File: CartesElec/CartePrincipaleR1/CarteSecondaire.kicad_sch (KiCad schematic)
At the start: 17 parts

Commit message: small updates
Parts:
- removed J? (x2): Conn_01x04_Male, symbol Connector:Conn_01x04_Male
- removed SW? (x2): SW_SPDT, symbol Switch:SW_SPDT
- added CONN_COL2: POMPE_1, Connector_JST:JST_XH_B2B-XH-A_1x02_P2.50mm_Vertical, symbol Connector:Conn_01x02_Male
- added CONN_COL3: POMPE_2, Connector_JST:JST_XH_B2B-XH-A_1x02_P2.50mm_Vertical, symbol Connector:Conn_01x02_Male
- added CONN_COL4, CONN_TIR2: Conn_01x02_Male, Connector_JST:JST_XH_B2B-XH-A_1x02_P2.50mm_Vertical, symbol Connector:Conn_01x02_Male
- added CONN_COL5: EV_1, Connector_JST:JST_XH_B2B-XH-A_1x02_P2.50mm_Vertical, symbol Connector:Conn_01x02_Male
- added CONN_COL6: EV_2, Connector_JST:JST_XH_B2B-XH-A_1x02_P2.50mm_Vertical, symbol Connector:Conn_01x02_Male
- added J17: Conn_01x02_Male, symbol Connector:Conn_01x02_Male
- added Q1, Q2, Q3, Q4: IRLML0030, Package_TO_SOT_SMD:SOT-23, symbol Transistor_FET:IRLML0030
- added R3, R5, R6, R7: R, symbol Device:R
- gave numbers to parts that had none: 13
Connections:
- net +12V: now also CONN_COL2.1 (Pin_1), CONN_COL3.1 (Pin_1), CONN_COL5.1 (Pin_1), CONN_COL6.1 (Pin_1), J17.1 (Pin_1)
- net GND: now also CONN_COL4.2 (Pin_2), CONN_TIR2.2 (Pin_2), J17.2 (Pin_2), Q1.2 (S), Q2.2 (S), Q3.2 (S), Q4.2 (S), R3.2, R5.2, R6.2, R7.2
- net DataAX12 renamed DataAX12_TX
- new net: Q3.1 (G), R6.1
- new net: CONN_COL5.2 (Pin_2), Q3.3 (D)
- new net: CONN_COL2.2 (Pin_2), Q1.3 (D)
- new net: CONN_COL6.2 (Pin_2), Q4.3 (D)
- new net: Q4.1 (G), R7.1
- new net: CONN_COL3.2 (Pin_2), Q2.3 (D)
- new net: Q1.1 (G), R3.1
- new net: Q2.1 (G), R5.1
- new net CONTACTEUR1_GPIO: CONN_COL4.1 (Pin_1)
- new net CONTACTEUR2_GPIO: CONN_TIR2.1 (Pin_1)
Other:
- moved on the sheet: J15, J16, J19, J21

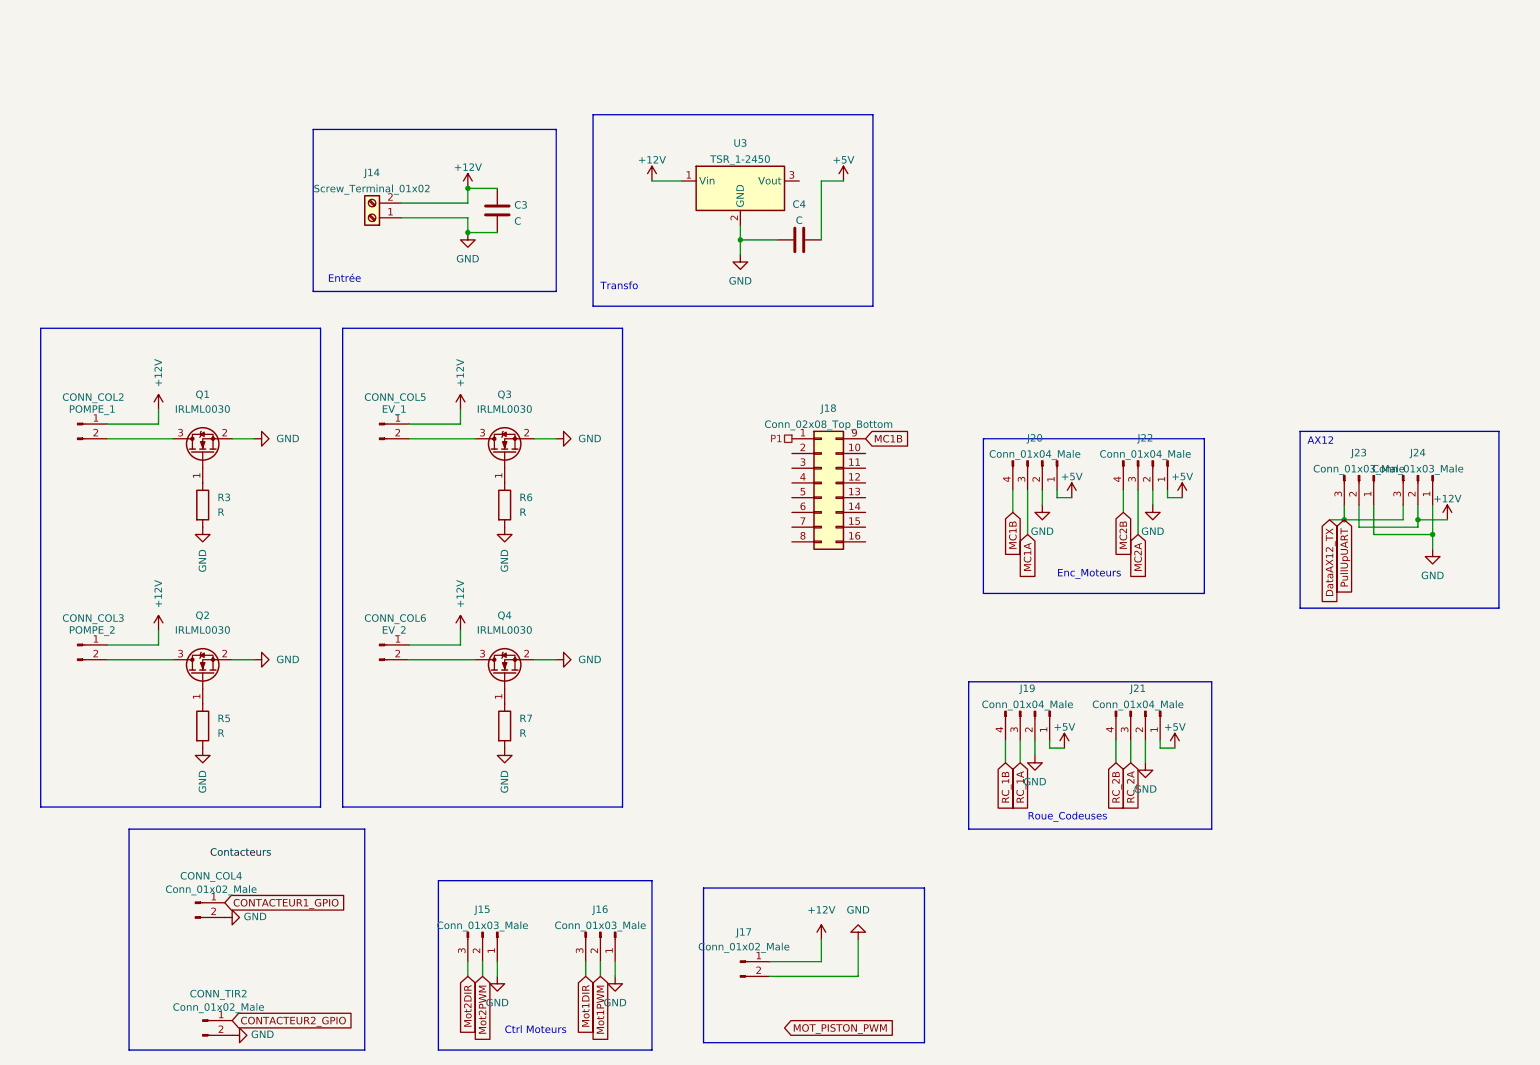
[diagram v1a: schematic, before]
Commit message: [carte robot 1] finish schematic.
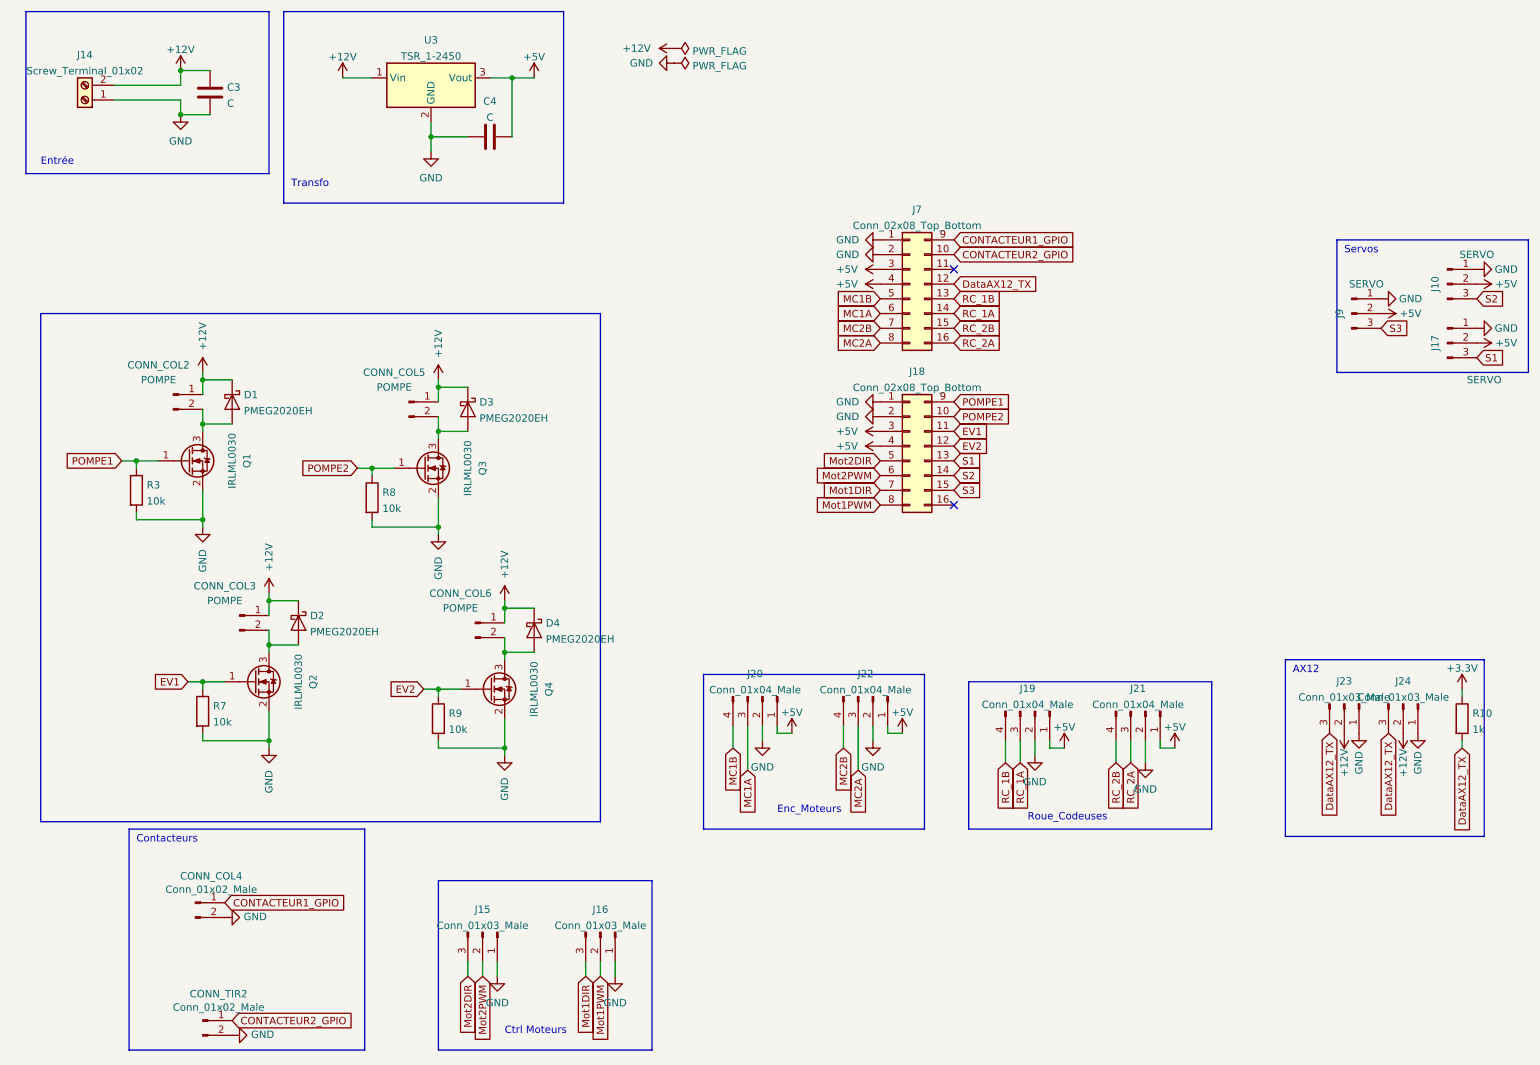
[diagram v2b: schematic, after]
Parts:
- removed J17: Conn_01x02_Male, symbol Connector:Conn_01x02_Male
- removed R5, R6: R, symbol Device:R
- added D1, D2, D3, D4: PMEG2020EH, Diode_SMD:D_SOD-123F, symbol Diode:PMEG2020EH
- added J10, J17, J9: SERVO, symbol Connector:Conn_01x03_Male
- added J7: Conn_02x08_Top_Bottom, symbol Connector_Generic:Conn_02x08_Top_Bottom
- added R10: 1k, symbol Device:R
- added R8, R9: 10k, symbol Device:R
- CONN_COL2: value POMPE_1 -> POMPE
- CONN_COL3: value POMPE_2 -> POMPE
- CONN_COL5: value EV_1 -> POMPE
- CONN_COL6: value EV_2 -> POMPE
- R3, R7: value R -> 10k
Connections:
- net P1 is gone; now on net GND: J18.1 (Pin_1)
- net +12V: now also D1.1 (K), D2.1 (K), D3.1 (K), D4.1 (K)
- net +5V: now also J18.3 (Pin_3), J18.4 (Pin_4), U3.3 (Vout), J10.2 (Pin_2), J17.2 (Pin_2), J7.3 (Pin_3), J7.4 (Pin_4), J9.2 (Pin_2)
- net CONTACTEUR1_GPIO: now also J7.9 (Pin_9)
- net CONTACTEUR2_GPIO: now also J7.10 (Pin_10)
- net DataAX12_TX: now also J7.12 (Pin_12), R10.2
- net GND: now also J18.2 (Pin_2), J10.1 (Pin_1), J17.1 (Pin_1), J7.1 (Pin_1), J7.2 (Pin_2), J9.1 (Pin_1), R8.2, R9.2
- net MC1A: now also J7.6 (Pin_6)
- net MC1B: now also J7.5 (Pin_5); no longer J18.9 (Pin_9)
- net MC2A: now also J7.8 (Pin_8)
- net MC2B: now also J7.7 (Pin_7)
- net Mot1DIR: now also J18.7 (Pin_7)
- net Mot1PWM: now also J18.8 (Pin_8)
- net Mot2DIR: now also J18.5 (Pin_5)
- net Mot2PWM: now also J18.6 (Pin_6)
- net RC_1A: now also J7.14 (Pin_14)
- net RC_1B: now also J7.13 (Pin_13)
- net RC_2A: now also J7.16 (Pin_16)
- net RC_2B: now also J7.15 (Pin_15)
- net POMPE2: now reaches J18.10 (Pin_10)
- net POMPE2: now also Q3.1 (G), R8.1
- net EV1: now reaches J18.11 (Pin_11)
- net EV1: now also Q2.1 (G), R7.1
- net EV2: now reaches J18.12 (Pin_12)
- net EV2: now also Q4.1 (G), R9.1
- net S1: now reaches J18.13 (Pin_13)
- net S1: now also J17.3 (Pin_3)
- net S2: now reaches J18.14 (Pin_14)
- net S2: now also J10.3 (Pin_3)
- net S3: now reaches J18.15 (Pin_15)
- net S3: now also J9.3 (Pin_3)
- net at CONN_COL5.2 (Pin_2), Q3.3 (D): now also D3.2 (A)
- net at CONN_COL2.2 (Pin_2), Q1.3 (D): now also D1.2 (A)
- net at CONN_COL6.2 (Pin_2), Q4.3 (D): now also D4.2 (A)
- net at CONN_COL3.2 (Pin_2), Q2.3 (D): now also D2.2 (A)
- net POMPE1: now reaches Q1.1 (G), R3.1
- net POMPE1: now also J18.9 (Pin_9)
- new net +3V3: R10.1
- no-connect marks 0 -> 2
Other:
- note added: "Contacteurs"
- note added: "Servos"
- moved on the sheet: C3, CONN_COL2, J14, J18, J20, J22, J23, J24, Q1, R3

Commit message: Add HE14 footprints.
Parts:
- CONN_COL2: footprint Connector_JST:JST_XH_B2B-XH-A_1x02_P2.50mm_Vertical -> library:HE14_EMBASE_1x02
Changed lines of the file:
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@@
     (property "Reference" "CONN_COL2" (id 0) (at 38.1 74.93 0))
     (property "Value" "POMPE" (id 1) (at 38.1 77.47 0))
-    (property "Footprint" "Connector_JST:JST_XH_B2B-XH-A_1x02_P2.50mm_Vertical" (id 2) (at 40.64 80.01 0)
+    (property "Footprint" "library:HE14_EMBASE_1x02" (id 2) (at 40.64 80.01 0)
       (effects (font (size 1.27 1.27)) hide)
     )

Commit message: carte secondair update
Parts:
- C3, C4: footprint (none) -> Capacitor_SMD:C_0805_2012Metric
- CONN_COL2: value POMPE -> POMPE1
- CONN_COL3: value POMPE -> EV1; footprint Connector_JST:JST_XH_B2B-XH-A_1x02_P2.50mm_Vertical -> library:HE14_EMBASE_1x02
- CONN_COL4: value Conn_01x02_Male -> CONTACT_1; footprint Connector_JST:JST_XH_B2B-XH-A_1x02_P2.50mm_Vertical -> library:HE14_EMBASE_1x02
- CONN_COL5: value POMPE -> POMPE2; footprint Connector_JST:JST_XH_B2B-XH-A_1x02_P2.50mm_Vertical -> library:HE14_EMBASE_1x02
- CONN_COL6: value POMPE -> EV2; footprint Connector_JST:JST_XH_B2B-XH-A_1x02_P2.50mm_Vertical -> library:HE14_EMBASE_1x02
- CONN_TIR2: value Conn_01x02_Male -> CONTACT_2; footprint Connector_JST:JST_XH_B2B-XH-A_1x02_P2.50mm_Vertical -> library:HE14_EMBASE_1x02
- J10: value SERVO -> SERVO2; footprint (none) -> Connector_PinHeader_2.54mm:PinHeader_1x03_P2.54mm_Vertical
- J14: footprint (none) -> TerminalBlock:TerminalBlock_bornier-2_P5.08mm
- J15: value Conn_01x03_Male -> MOT_PWM_2; footprint (none) -> library:HE14_EMBASE_1x03
- J16: value Conn_01x03_Male -> MOT_PWM_1; footprint (none) -> library:HE14_EMBASE_1x03
- J17: value SERVO -> SERVO1; footprint (none) -> Connector_PinHeader_2.54mm:PinHeader_1x03_P2.54mm_Vertical
- J18, J7: footprint (none) -> Connector_IDC:IDC-Header_2x08_P2.54mm_Vertical
- J19: value Conn_01x04_Male -> ENC_FOL_1; footprint (none) -> library:HE14_EMBASE_1x04
- J20: value Conn_01x04_Male -> ENC_MOT_1; footprint (none) -> library:HE14_EMBASE_1x04
- J21: value Conn_01x04_Male -> ENC_FOL_2; footprint (none) -> library:HE14_EMBASE_1x04
- J22: value Conn_01x04_Male -> ENC_MOT_2; footprint (none) -> library:HE14_EMBASE_1x04
- J23: value Conn_01x03_Male -> AX12_1; footprint (none) -> Connector_Molex:Molex_SPOX_5267-03A_1x03_P2.50mm_Vertical
- J24: value Conn_01x03_Male -> AX12_2; footprint (none) -> Connector_Molex:Molex_SPOX_5267-03A_1x03_P2.50mm_Vertical
- J9: value SERVO -> SERVO3; footprint (none) -> Connector_PinHeader_2.54mm:PinHeader_1x03_P2.54mm_Vertical
- R10, R3, R7, R8, R9: footprint (none) -> Resistor_SMD:R_0805_2012Metric
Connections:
- net +3V3: now also J18.16 (Pin_16)
- net CONTACTEUR1_GPIO: now also J7.10 (Pin_10); no longer J7.9 (Pin_9)
- net CONTACTEUR2_GPIO: now also J7.9 (Pin_9); no longer J7.10 (Pin_10)
- net EV1: now also J18.12 (Pin_12); no longer J18.11 (Pin_11)
- net EV2: now also J18.11 (Pin_11); no longer J18.12 (Pin_12)
- net POMPE1: now also J18.10 (Pin_10); no longer J18.9 (Pin_9)
- net POMPE2: now also J18.9 (Pin_9); no longer J18.10 (Pin_10)
- net RC_2A: now also J7.15 (Pin_15); no longer J7.16 (Pin_16)
- net RC_2B: now also J7.16 (Pin_16); no longer J7.15 (Pin_15)
- no-connect marks 2 -> 1
